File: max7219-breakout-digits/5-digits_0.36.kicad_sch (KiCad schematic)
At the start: 5 parts, among them J1 Conn_02x08_Odd_Even, U1 HDSM-443B_7-Segment_3_Digit, U2 HDSM-443B_7-Segment_3_Digit

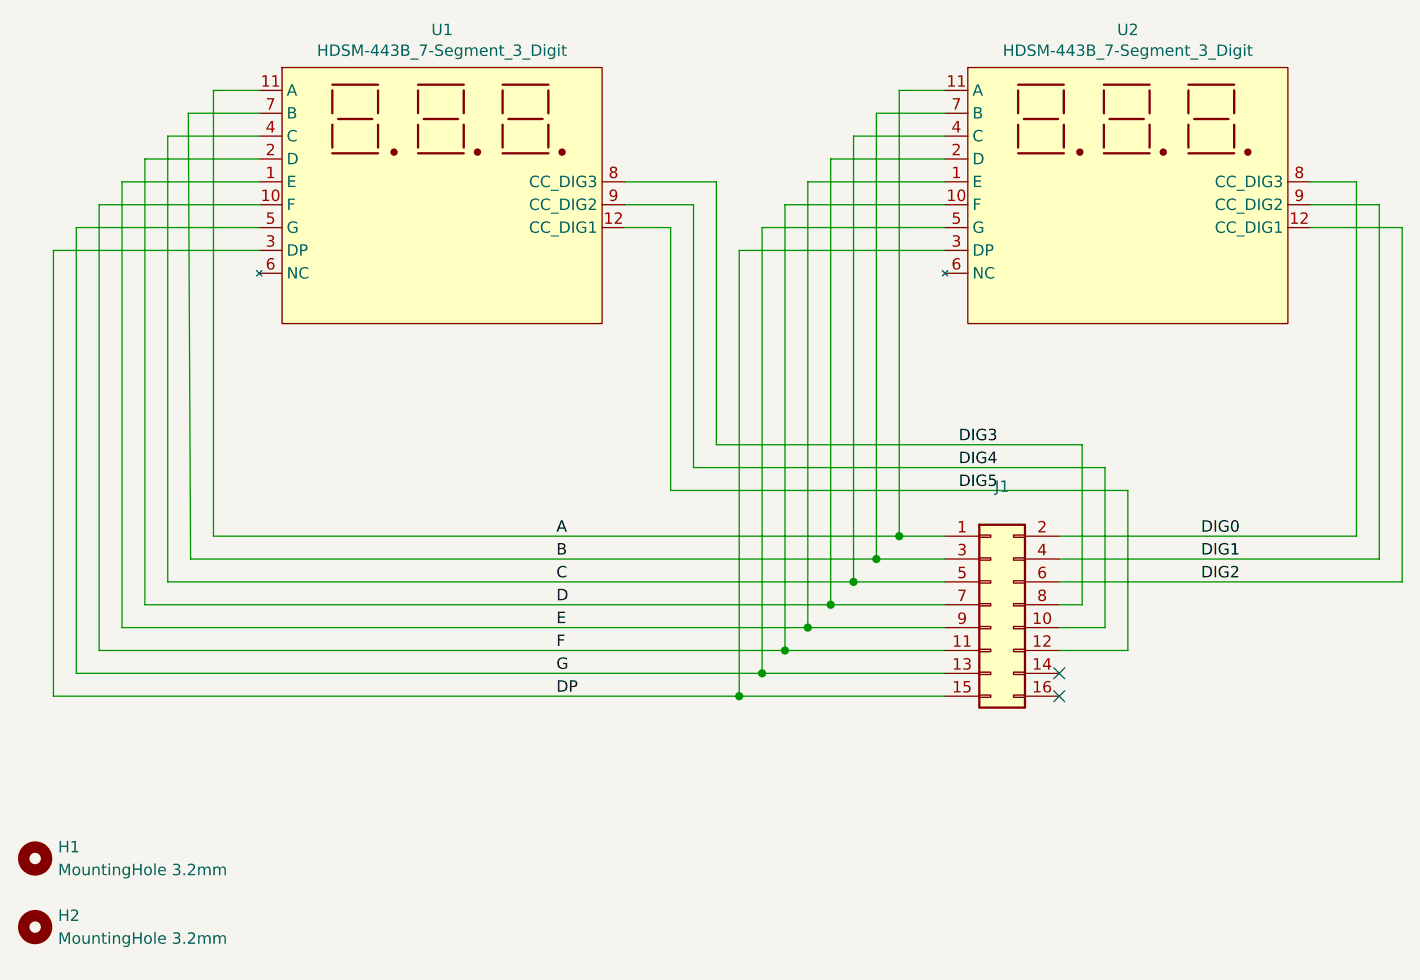
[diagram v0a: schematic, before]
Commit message: rename everything from 0.35 to 0.36
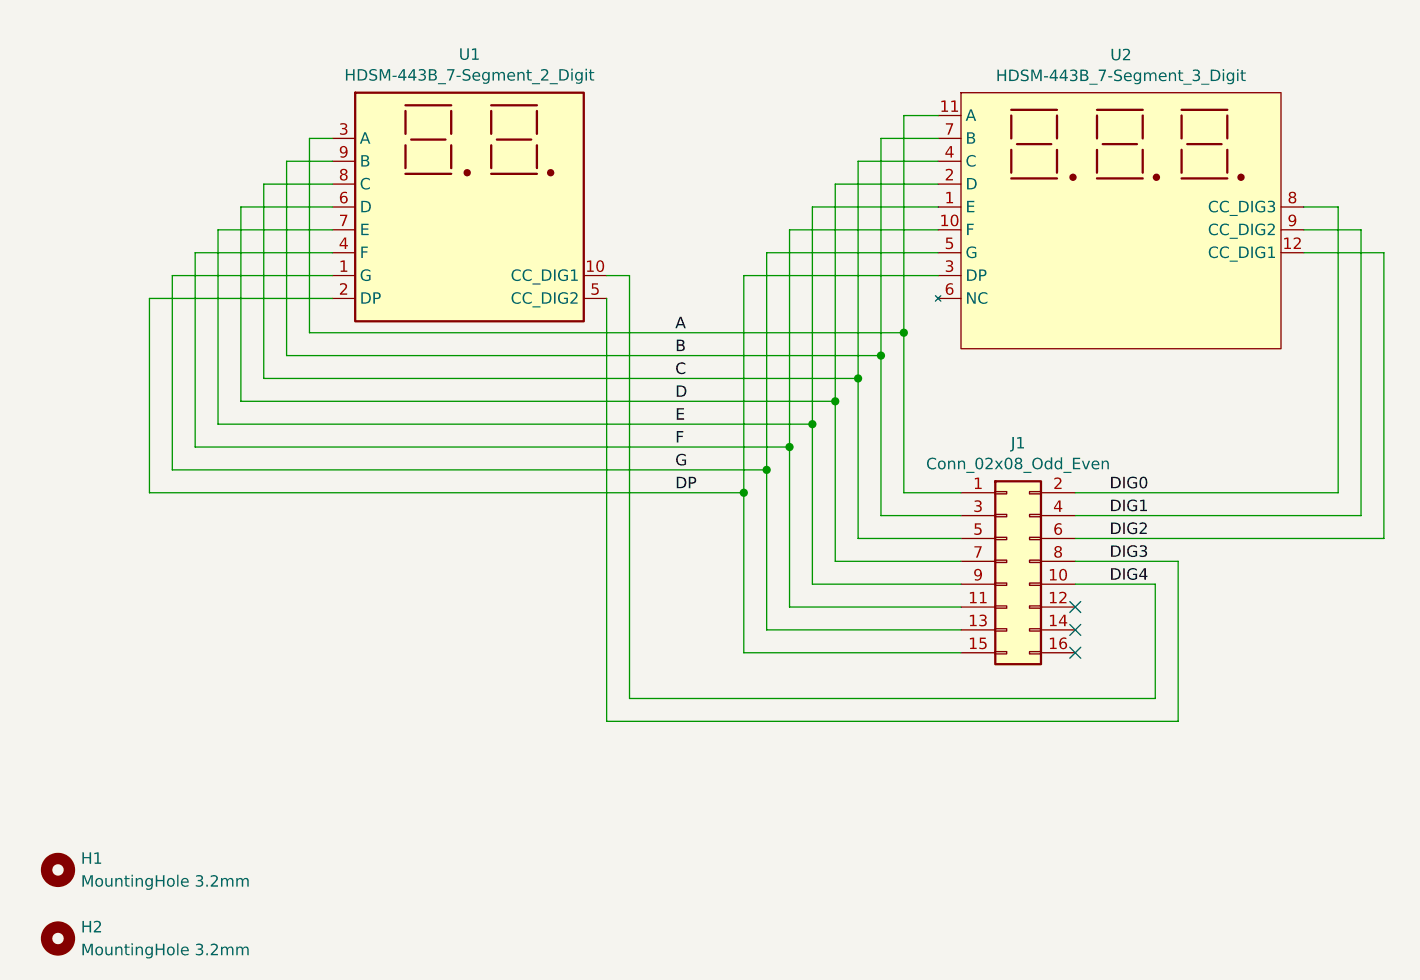
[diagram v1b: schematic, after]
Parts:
- removed U1, U2: HDSM-443B_7-Segment_3_Digit, MobiFlight:STH_7_3 Digits_0.35_CC, symbol MobiFlight:7Segment 3 digit 0.35 common cathode STH
- added U1: HDSM-443B_7-Segment_2_Digit, MobiFlight:STH_7_2 Digits_0.36_CC, symbol MobiFlight:7Segment 2 digit 0.36 common cathode STH
- added U2: HDSM-443B_7-Segment_3_Digit, MobiFlight:STH_7_3 Digits_0.36_CC, symbol MobiFlight:7Segment 3 digit 0.36 common cathode STH
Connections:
- net A: now also U1.3 (A), U2.11 (A)
- net B: now also U1.9 (B), U2.7 (B)
- net C: now also U1.8 (C), U2.4 (C)
- net D: now also U1.6 (D), U2.2 (D)
- net DIG0: now also U2.8 (CC_DIG3)
- net DIG1: now also U2.9 (CC_DIG2)
- net DIG2: now also U2.12 (CC_DIG1)
- net DIG3: now also U1.5 (CC_DIG2)
- net DIG4: now also U1.10 (CC_DIG1)
- net DP: now also U1.2 (DP), U2.3 (DP)
- net E: now also U1.7 (E), U2.1 (E)
- net F: now also U1.4 (F), U2.10 (F)
- net G: now also U1.1 (G), U2.5 (G)
- net DIG5: no longer names the net of J1.12 (Pin_12)
- no-connect marks 2 -> 3
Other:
- title: 7-Segment Display Module 0.35, 6 Digits -> 7-Segment Display Module 0.36, 5 Digits
